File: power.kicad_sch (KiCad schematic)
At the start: 13 parts, among them P1 USB_C_Plug_USB2.0, U2 MAX17048G, U3 BQ24090DGQ, U4 TPS7A0508PDBZ

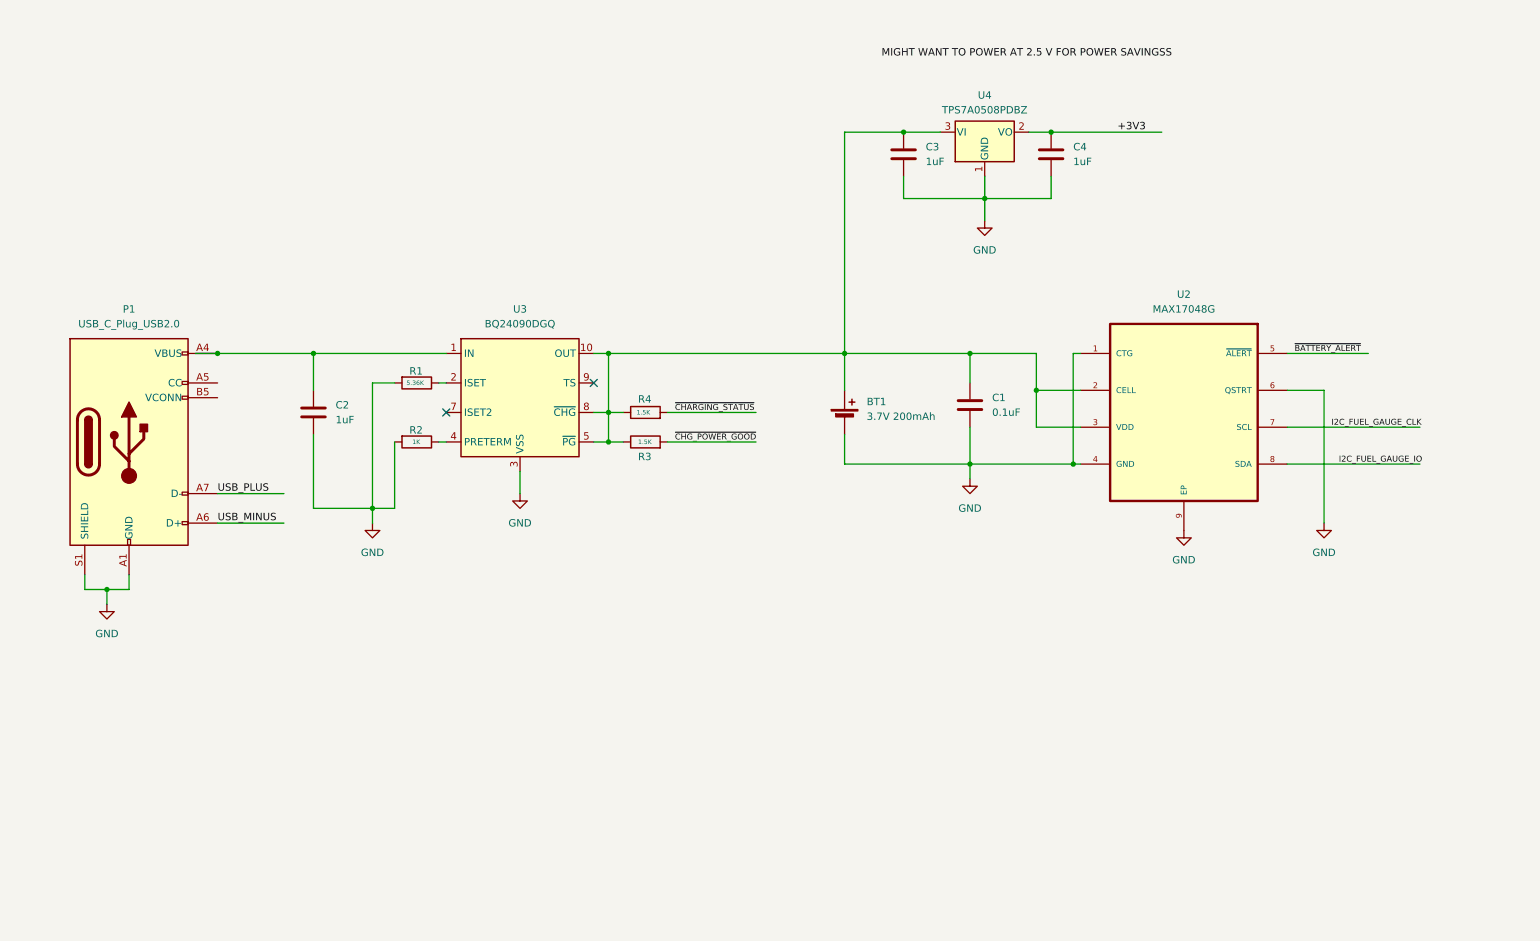
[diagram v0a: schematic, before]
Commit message: added eink conn page
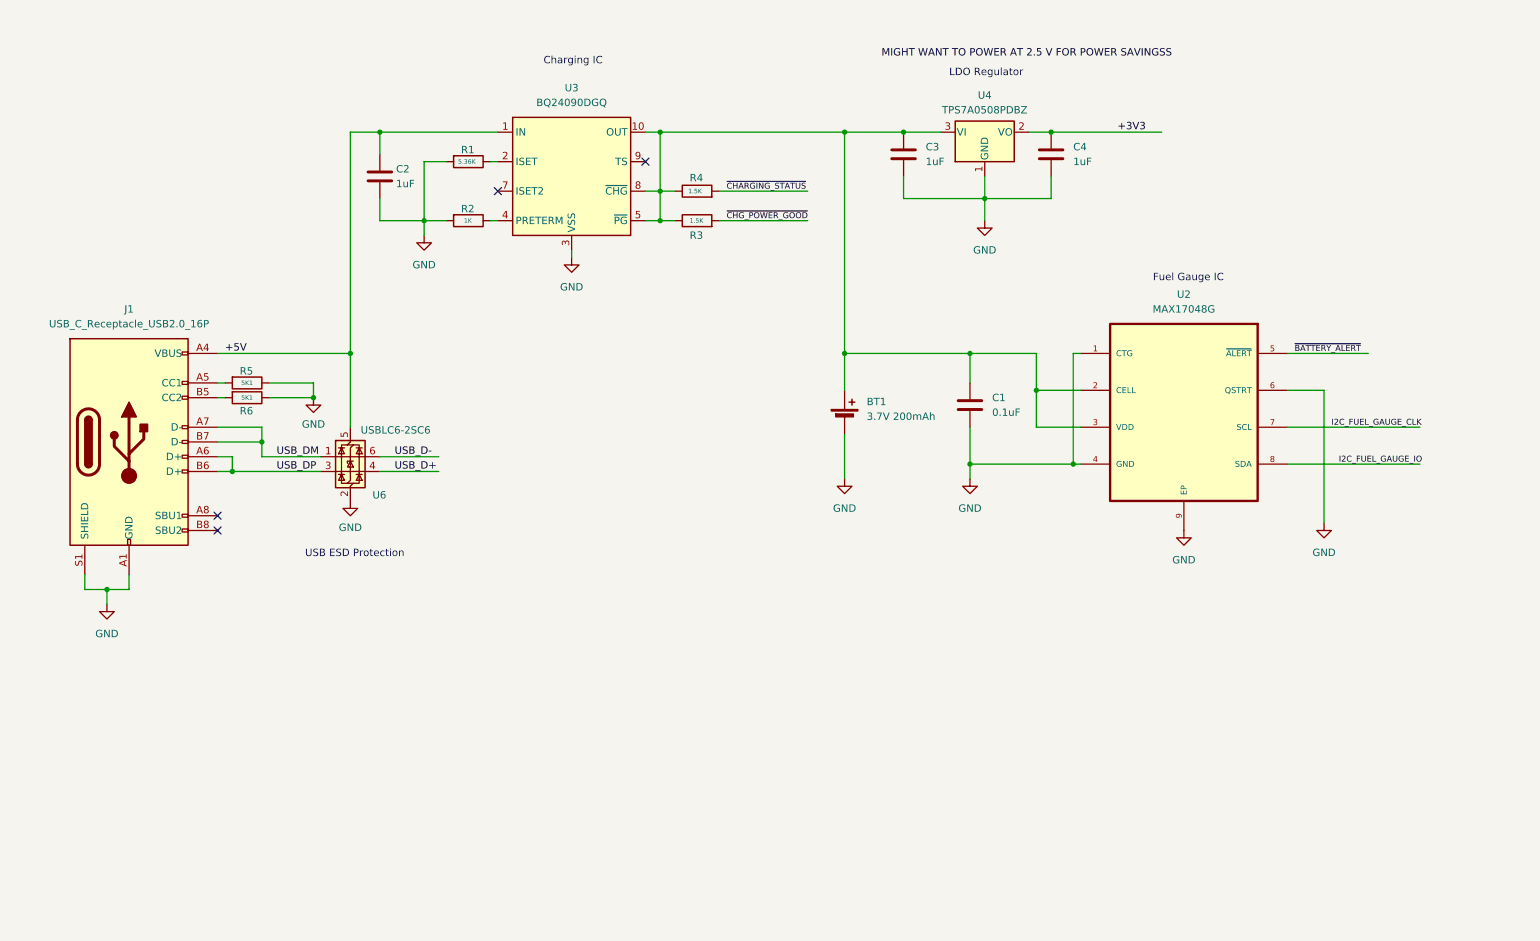
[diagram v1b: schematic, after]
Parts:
- removed P1: USB_C_Plug_USB2.0, symbol Connector:USB_C_Plug_USB2.0
- added J1: USB_C_Receptacle_USB2.0_16P, symbol Connector:USB_C_Receptacle_USB2.0_16P
- added R5, R6: 5K1, symbol Device:R
- added U6: USBLC6-2SC6, Package_TO_SOT_SMD:SOT-23-6, symbol Power_Protection:USBLC6-2SC6
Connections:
- net GND: now also J1.A1 (GND), J1.A12 (GND), J1.B1 (GND), J1.B12 (GND), J1.S1 (SHIELD), R5.1, R6.1, U6.2 (GND)
- net +5V: now reaches C2.1, U3.1 (IN)
- net +5V: now also J1.A4 (VBUS), J1.A9 (VBUS), J1.B4 (VBUS), J1.B9 (VBUS), U6.5 (VBUS)
- new net: J1.A5 (CC1), R5.2
- new net: J1.B5 (CC2), R6.2
- new net USB_D+: U6.4 (I/O2)
- new net USB_D-: U6.6 (I/O1)
- new net USB_DM: J1.A7 (D-), J1.B7 (D-), U6.1 (I/O1)
- new net USB_DP: J1.A6 (D+), J1.B6 (D+), U6.3 (I/O2)
- no-connect marks 2 -> 4
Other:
- note added: "Charging IC"
- note added: "Fuel Gauge IC"
- note added: "LDO Regulator"
- note added: "USB ESD Protection"
- moved on the sheet: C2, R1, R2, R3, R4, U3

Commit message: added decoupling caps on mcu
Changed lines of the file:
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@@
-		)
-	)
-	(label "+3V3"
-		(at 203.2 40.64 0)
-		(effects
-			(font
-				(size 1.27 1.27)
-			)
-			(justify left bottom)
 		)
 	)
@@
 					(unit 1)
 				)
+			)
+		)
+	)
+	(symbol
+		(lib_id "power:+3V3")
+		(at 210.82 40.64 270)
+		(unit 1)
+		(exclude_from_sim no)
+		(in_bom yes)
+		(on_board yes)
+		(dnp no)
+		(fields_autoplaced yes)
+		(property "Reference" "#PWR020"
+			(at 207.01 40.64 0)
+			(effects
+				(font
+					(size 1.27 1.27)
+				)
+				(hide yes)
+			)
+		)
+		(property "Value" "+3V3"
+			(at 214.63 40.6399 90)
+			(effects
+				(font
+					(size 1.27 1.27)
+				)
+				(justify left)
+			)
+		)
+		(property "Footprint" ""
+			(at 210.82 40.64 0)
+			(effects
+				(font
+					(size 1.27 1.27)
+				)
+				(hide yes)
+			)
+		)
+		(property "Datasheet" ""
+			(at 210.82 40.64 0)
+			(effects
+				(font
+					(size 1.27 1.27)
+				)
+				(hide yes)
+			)
+		)
+		(property "Description" "Power symbol creates a global label with name \"+3V3\""
+			(at 210.82 40.64 0)
+			(effects
+				(font
+					(size 1.27 1.27)
+				)
+				(hide yes)
+			)
+		)
+		(pin "1"
+		)
+		(instances
+			(project ""
+				(path "/29eb74dc-e91c-4cc5-ad9f-7f8caf36d690/50aa898a-4cd9-4f6c-a569-964480767df5"
+					(reference "#PWR020")
+					(unit 1)
+				)

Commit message: cleaned up rf & connected boot0
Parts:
- R1: value 5.36K -> 5K36
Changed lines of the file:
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@@
 			)
 		)
-		(property "Value" "5.36K"
-			(at 89.662 45.72 90)
-			(effects
-				(font
-					(size 0.762 0.762)
+		(property "Value" "5K36"
+			(at 89.154 48.26 90)
+			(effects
+				(font
+					(size 1.27 1.27)
 				)
 				(justify left)
@@
 		)
 		(property "Value" "1K"
-			(at 90.678 55.88 90)
-			(effects
-				(font
-					(size 0.762 0.762)
+			(at 90.424 58.166 90)
+			(effects
+				(font
+					(size 1.27 1.27)
 				)
 				(justify left)
@@
 		(dnp no)
 		(property "Reference" "R6"
-			(at 52.07 88.646 90)
+			(at 56.134 87.63 90)
 			(effects
 				(font
@@
 		)
 		(property "Value" "5K1"
-			(at 52.324 86.36 90)
-			(effects
-				(font
-					(size 0.762 0.762)
+			(at 51.562 88.646 90)
+			(effects
+				(font
+					(size 1.27 1.27)
 				)
 				(justify left)
@@
 		(dnp no)
 		(property "Reference" "R5"
-			(at 52.07 81.788 90)
+			(at 56.134 82.55 90)
 			(effects
 				(font
@@
 		)
 		(property "Value" "5K1"
-			(at 52.324 83.82 90)
-			(effects
-				(font
-					(size 0.762 0.762)
-				)
-				(justify left)
+			(at 51.308 81.788 90)
+			(effects
+				(font
+					(size 1.27 1.27)
+				)
+				(justify left)

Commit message: Added external flash ic & 4 push buttons
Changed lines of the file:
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@@
+	(wire
+		(pts
+			(xy 205.74 40.64) (xy 191.77 40.64)
+		)
+		(stroke
+			(width 0)
+			(type default)
+		)
+	)
 	(wire
 		(pts
@@
 	(wire
 		(pts
-			(xy 191.77 40.64) (xy 210.82 40.64)
-		)
-		(stroke
-			(width 0)
-			(type default)
-		)
-	)
-	(wire
-		(pts
 			(xy 71.12 40.64) (xy 76.2 40.64)
 		)
@@
 		(pts
 			(xy 29.21 119.38) (xy 33.02 119.38)
+		)
+		(stroke
+			(width 0)
+			(type default)
+		)
+	)
+	(wire
+		(pts
+			(xy 205.74 39.37) (xy 205.74 40.64)
 		)
 		(stroke
@@
 	(symbol
 		(lib_id "power:+3V3")
-		(at 210.82 40.64 270)
+		(at 205.74 39.37 0)
 		(unit 1)
 		(exclude_from_sim no)
@@
 		(fields_autoplaced yes)
 		(property "Reference" "#PWR020"
-			(at 207.01 40.64 0)
+			(at 205.74 43.18 0)
 			(effects
 				(font
@@
 		)
 		(property "Value" "+3V3"
-			(at 214.63 40.6399 90)
-			(effects
-				(font
-					(size 1.27 1.27)
-				)
-				(justify left)
+			(at 205.74 34.29 0)
+			(effects
+				(font
+					(size 1.27 1.27)
+				)
 			)
 		)
 		(property "Footprint" ""
-			(at 210.82 40.64 0)
+			(at 205.74 39.37 0)
 			(effects
 				(font
@@
 		)
 		(property "Datasheet" ""
-			(at 210.82 40.64 0)
+			(at 205.74 39.37 0)
 			(effects
 				(font
@@
 		)
 		(property "Description" "Power symbol creates a global label with name \"+3V3\""
-			(at 210.82 40.64 0)
-			(effects
-				(font
+			(at 205.74 39.37 0)
+			(effects
+				(font

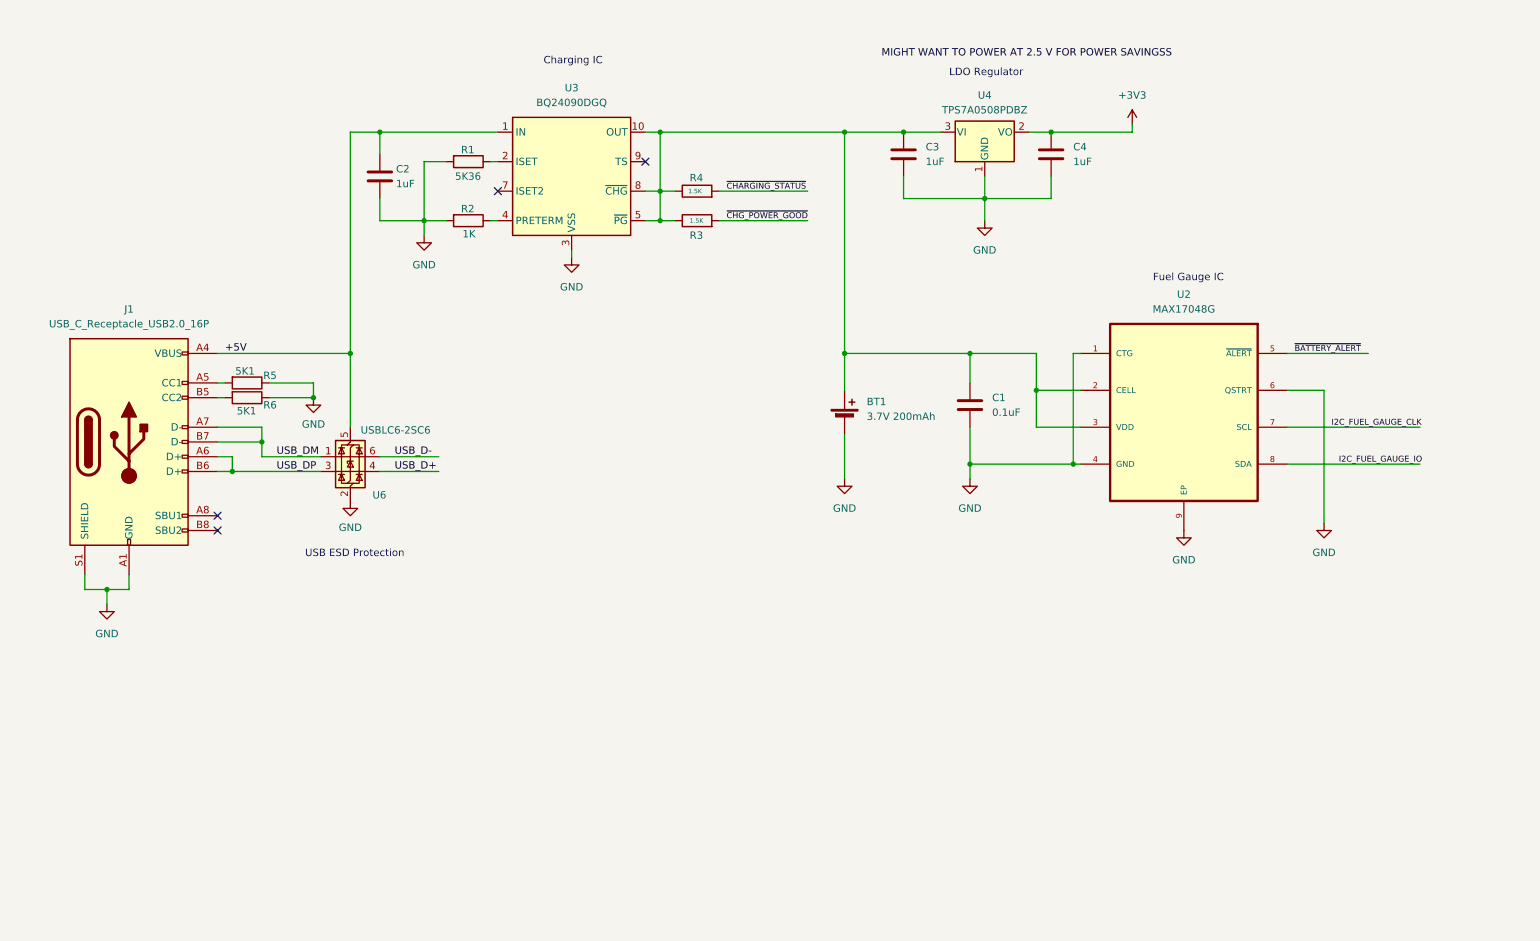
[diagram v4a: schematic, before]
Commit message: cleaned up some net labels for ERC
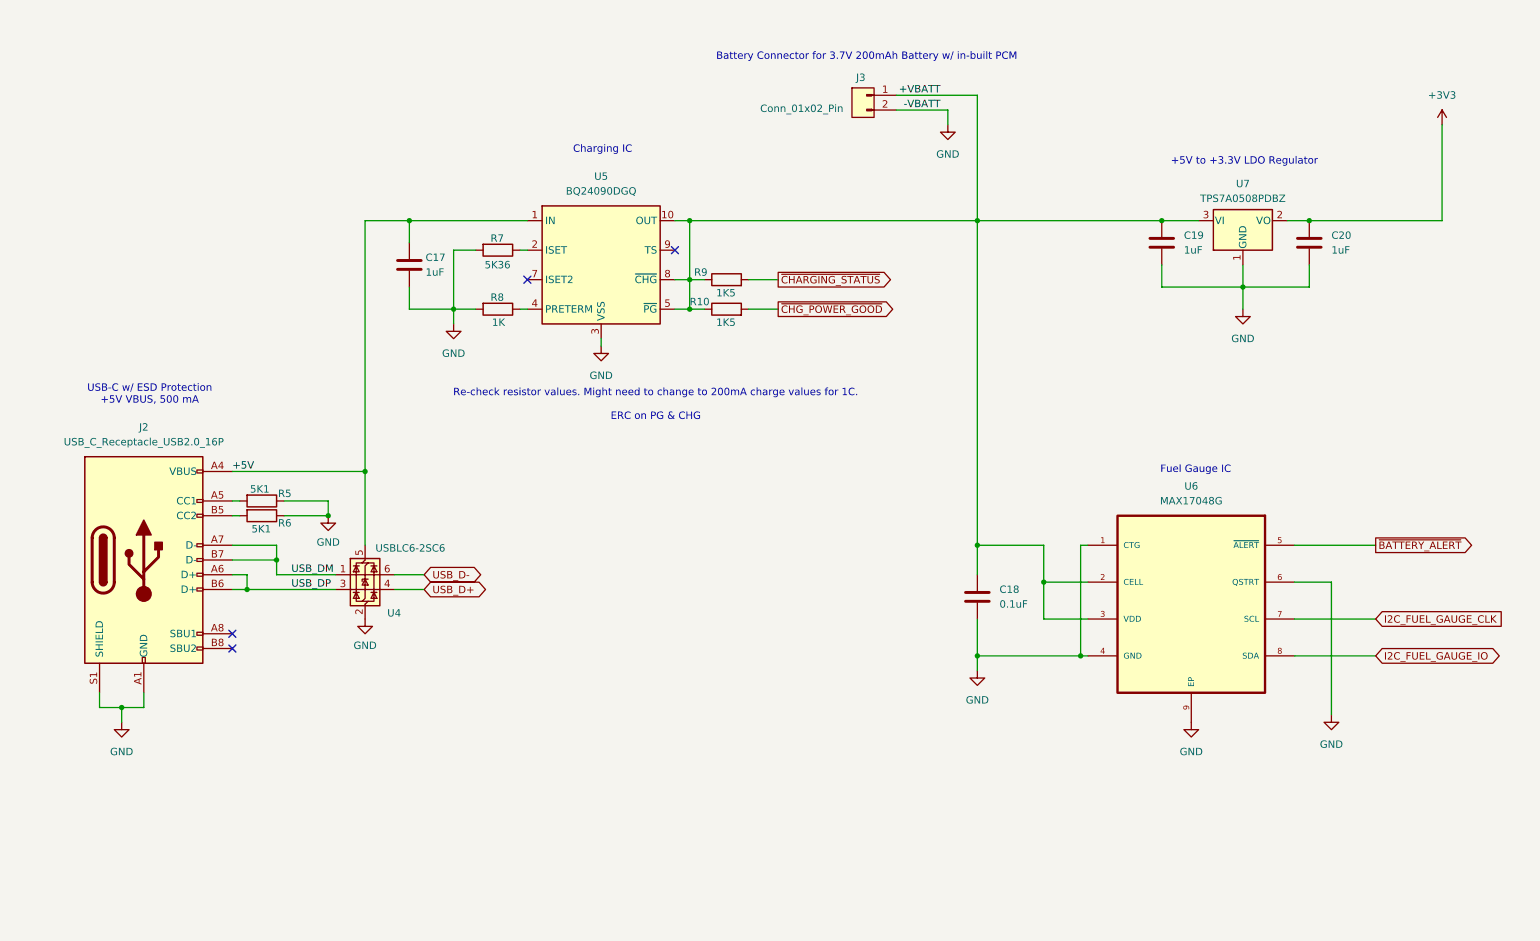
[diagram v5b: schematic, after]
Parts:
- removed BT1: 3.7V 200mAh, symbol Device:Battery_Cell
- added J3: Conn_01x02_Pin, symbol Connector:Conn_01x02_Pin
- R10: renamed from R3; value 1.5K -> 1K5
- R9: renamed from R4; value 1.5K -> 1K5
- renumbered C2 to C17, C1 to C18, C3 to C19, C4 to C20, J1 to J2, R1 to R7, R2 to R8, U6 to U4, U3 to U5, U2 to U6, U4 to U7
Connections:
- net GND: now also J3.2 (Pin_2)
- net +VBATT: now reaches C18.1, C19.1, R10.1, R9.1, U5.10 (OUT), U5.5 (~{PG}), U5.8 (~{CHG}), U6.2 (CELL), U6.3 (VDD), U7.3 (VI)
- net +VBATT: now also J3.1 (Pin_1)
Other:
- note added: "+5V to +3.3V LDO Regulator"
- note added: "Battery Connector for 3.7V 200mAh Battery w/ in-built PCM"
- note added: "Re-check resistor values. Might need to change to 200mA charge values for 1C. ERC on PG & CHG"
- note added: "USB-C w/ ESD Protection +5V VBUS, 500 mA"
- note removed: "LDO Regulator"
- note removed: "USB ESD Protection"
- moved on the sheet: C17, C18, C19, C20, J2, R10, R5, R6, R7, R8, R9, U4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
